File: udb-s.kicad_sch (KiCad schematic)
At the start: 10 parts, among them J1 TYPE-C-31-M-12, J2 78171-0004, U1 TPD4E05U06DQAR

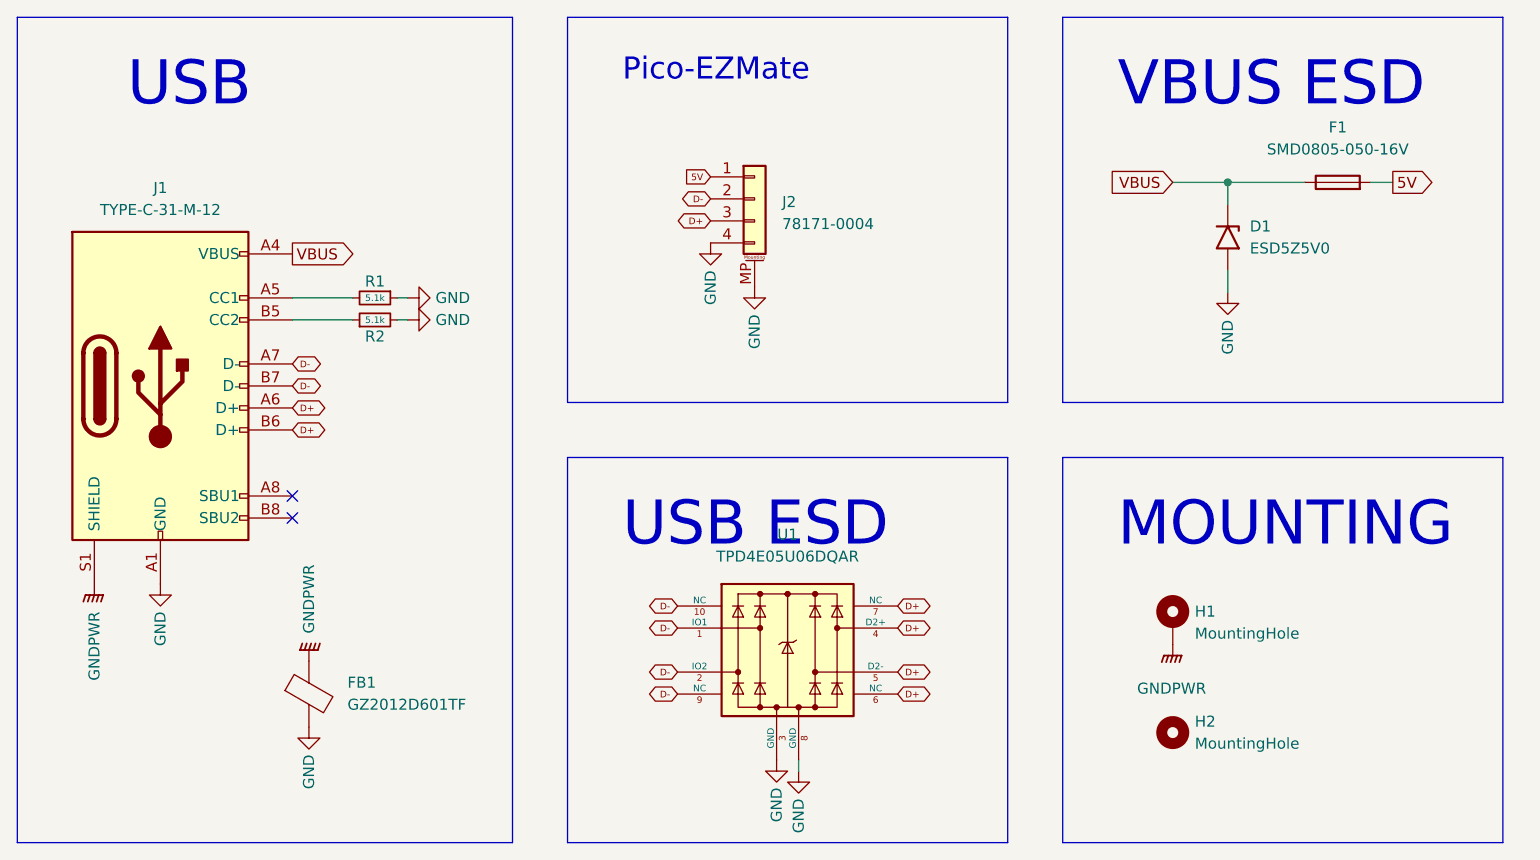
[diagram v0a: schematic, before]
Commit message: mods for jst-sh
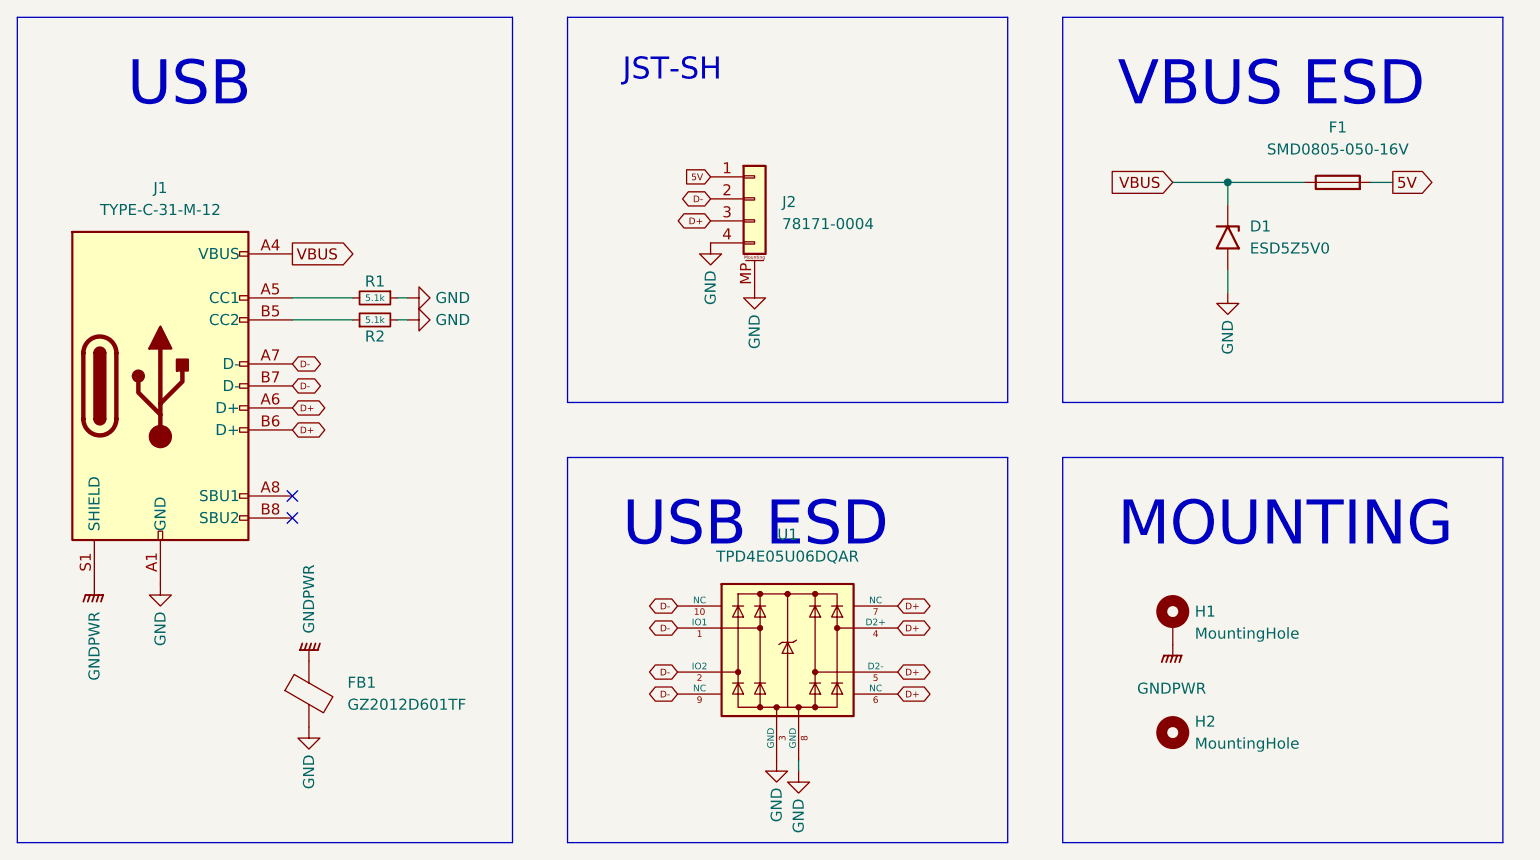
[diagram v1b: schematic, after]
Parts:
- J2: footprint locallib:PicoEZMate-Reinforced-Lite -> Connector_JST:JST_SH_SM04B-SRSS-TB_1x04-1MP_P1.00mm_Horizontal; LCSC Part Number C588524 -> C7430446; Manufacturer MOLEX -> Megastar; Manufacturer Part Number 78171-0004 -> ZX-SH1.0-4PWT
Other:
- note added: "JST-SH"
- note removed: "Pico-EZMate"

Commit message: v2
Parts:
- J2: value 78171-0004 -> ZX-SH1.0-4PWT
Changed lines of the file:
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@@
   (symbol (lib_id "Connector_Generic_MountingPin:Conn_01x04_MountingPin") (at 173.99 46.355 0) (unit 1)
     (in_bom yes) (on_board yes) (dnp no) (fields_autoplaced)
-    (property "Reference" "J2" (at 177.165 46.7105 0)
+    (property "Reference" "J2" (at 176.022 47.3369 0)
       (effects (font (size 1.27 1.27)) (justify left))
     )
-    (property "Value" "78171-0004" (at 177.165 49.2505 0)
+    (property "Value" "ZX-SH1.0-4PWT" (at 176.022 49.2579 0)
       (effects (font (size 1.27 1.27)) (justify left))
     )
